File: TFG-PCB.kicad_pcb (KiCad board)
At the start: 2 copper layers, 287.3 x 99.2 mm, 141 parts, among them J1 TYPE-C-31-M-12, SW1 SW_Push, U1 ATmega32U4-AU, Y1 16MHz

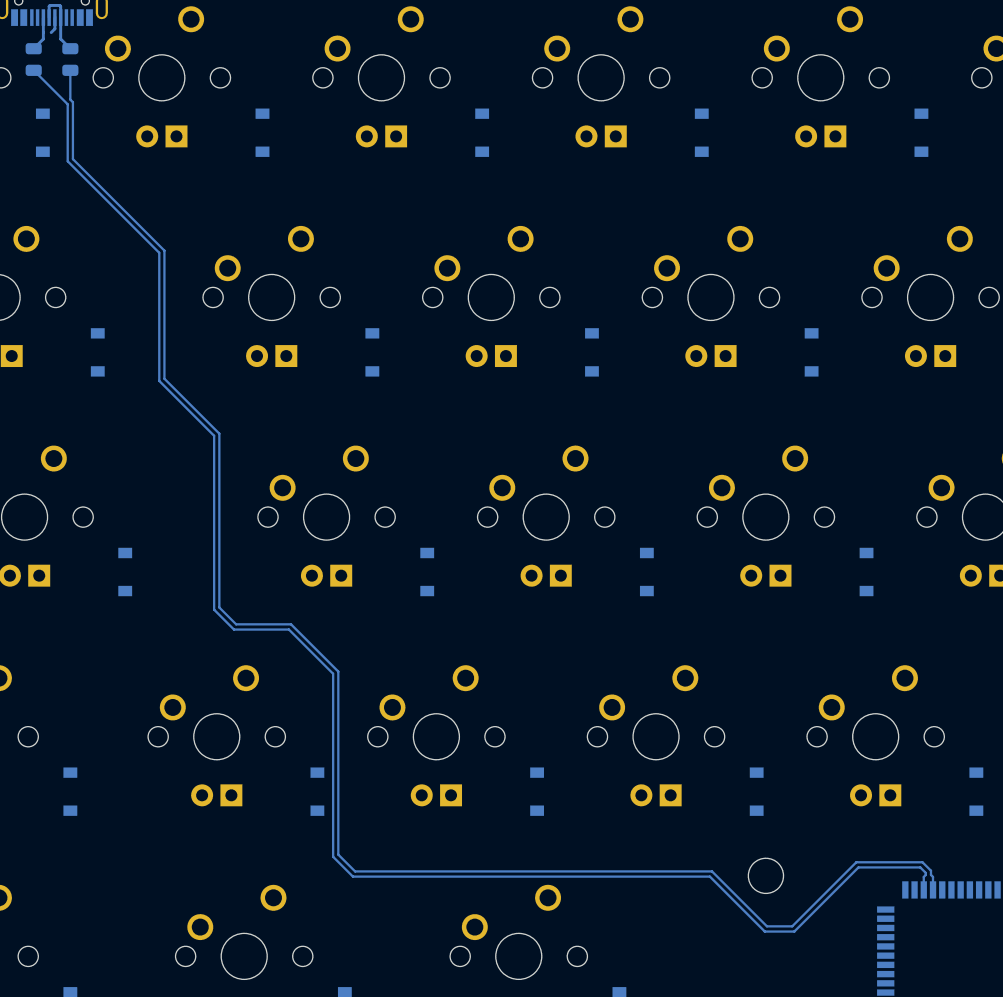
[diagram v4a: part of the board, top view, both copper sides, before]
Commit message: Wired USB
Finished differential wiring + skew
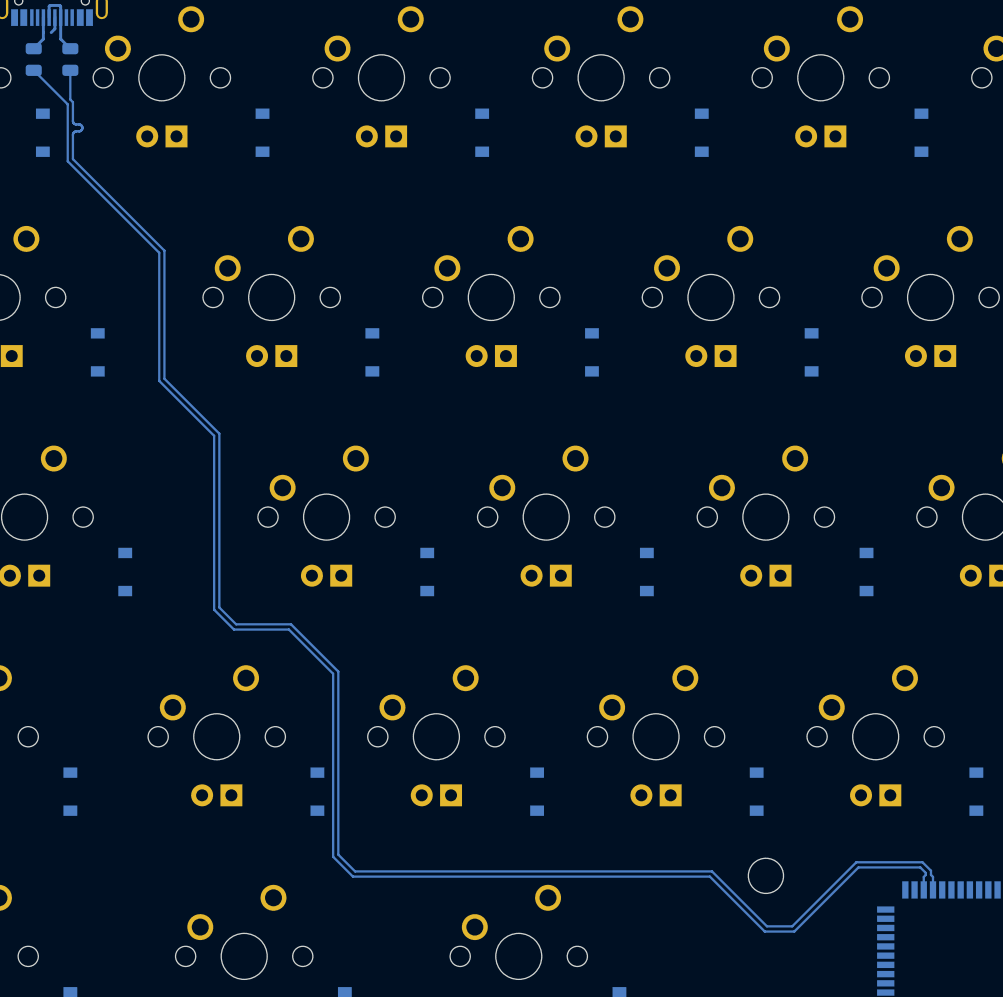
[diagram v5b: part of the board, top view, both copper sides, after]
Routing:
- net /D_P: track 138.8 -> 139.9 mm
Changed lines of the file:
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@@
     (thickness 1.6)
     (drawings 466)
-    (tracks 64)
+    (tracks 95)
     (zones 0)
     (modules 141)
@@
   (segment (start 222.25 237.98125) (end 225.28125 237.98125) (width 0.254) (layer B.Cu) (net 44))
   (segment (start 225.28125 237.98125) (end 226.275 238.975) (width 0.254) (layer B.Cu) (net 44))
-  (segment (start 150.11195 211.70625) (end 148.65625 210.25055) (width 0.2) (layer B.Cu) (net 122))
-  (segment (start 154.87445 211.70625) (end 150.11195 211.70625) (width 0.2) (layer B.Cu) (net 122))
-  (segment (start 158.975 215.8068) (end 154.87445 211.70625) (width 0.2) (layer B.Cu) (net 122))
-  (segment (start 158.975 231.6818) (end 158.975 215.8068) (width 0.2) (layer B.Cu) (net 122))
-  (segment (start 160.4307 233.1375) (end 158.975 231.6818) (width 0.2) (layer B.Cu) (net 122))
-  (segment (start 198.3443 237.9) (end 196.14945 237.9) (width 0.2) (layer B.Cu) (net 122))
-  (segment (start 203.90055 232.34375) (end 198.3443 237.9) (width 0.2) (layer B.Cu) (net 122))
-  (segment (start 209.6432 232.34375) (end 203.90055 232.34375) (width 0.2) (layer B.Cu) (net 122))
-  (segment (start 191.38695 233.1375) (end 160.4307 233.1375) (width 0.2) (layer B.Cu) (net 122))
-  (segment (start 143.89375 179.2943) (end 135.95625 171.3568) (width 0.2) (layer B.Cu) (net 122))
-  (segment (start 210.5535 234.74275) (end 210.5535 233.617749) (width 0.2) (layer B.Cu) (net 122))
-  (segment (start 210.5535 233.617749) (end 210.3785 233.442749) (width 0.2) (layer B.Cu) (net 122))
-  (segment (start 210.3785 233.442749) (end 210.3785 233.07905) (width 0.2) (layer B.Cu) (net 122))
-  (segment (start 210.3785 233.07905) (end 209.6432 232.34375) (width 0.2) (layer B.Cu) (net 122))
-  (segment (start 148.65625 210.25055) (end 148.65625 195.1693) (width 0.2) (layer B.Cu) (net 122))
-  (segment (start 196.14945 237.9) (end 191.38695 233.1375) (width 0.2) (layer B.Cu) (net 122))
-  (segment (start 148.65625 195.1693) (end 143.89375 190.4068) (width 0.2) (layer B.Cu) (net 122))
-  (segment (start 143.89375 190.4068) (end 143.89375 179.2943) (width 0.2) (layer B.Cu) (net 122))
-  (segment (start 135.95625 171.3568) (end 135.95625 166.419853) (width 0.2) (layer B.Cu) (net 122))
-  (segment (start 135.95625 166.419853) (end 135.73125 166.194853) (width 0.2) (layer B.Cu) (net 122))
-  (segment (start 135.73125 166.194853) (end 135.73125 163.65625) (width 0.2) (layer B.Cu) (net 122))
+  (segment (start 158.975 231.6818) (end 160.4307 233.1375) (width 0.2) (layer B.Cu) (net 122))
+  (segment (start 209.6432 232.34375) (end 210.3785 233.07905) (width 0.2) (layer B.Cu) (net 122))
+  (segment (start 158.975 215.8068) (end 158.975 231.6818) (width 0.2) (layer B.Cu) (net 122))
+  (segment (start 196.14945 237.9) (end 198.3443 237.9) (width 0.2) (layer B.Cu) (net 122))
+  (segment (start 154.87445 211.70625) (end 158.975 215.8068) (width 0.2) (layer B.Cu) (net 122))
+  (segment (start 150.11195 211.70625) (end 154.87445 211.70625) (width 0.2) (layer B.Cu) (net 122))
+  (segment (start 210.5535 233.617749) (end 210.5535 234.74275) (width 0.2) (layer B.Cu) (net 122))
+  (segment (start 148.65625 210.25055) (end 150.11195 211.70625) (width 0.2) (layer B.Cu) (net 122))
+  (segment (start 143.89375 190.4068) (end 148.65625 195.1693) (width 0.2) (layer B.Cu) (net 122))
+  (segment (start 136.714674 168.462953) (end 136.750415 168.519834) (width 0.2) (layer B.Cu) (net 122))
+  (segment (start 136.667171 168.41545) (end 136.714674 168.462953) (width 0.2) (layer B.Cu) (net 122))
+  (segment (start 136.480124 168.35) (end 136.546881 168.357521) (width 0.2) (layer B.Cu) (net 122))
+  (segment (start 136.069204 168.284549) (end 136.126085 168.32029) (width 0.2) (layer B.Cu) (net 122))
+  (segment (start 136.25625 168.35) (end 136.480124 168.35) (width 0.2) (layer B.Cu) (net 122))
+  (segment (start 136.126085 168.32029) (end 136.189494 168.342478) (width 0.2) (layer B.Cu) (net 122))
+  (segment (start 203.90055 232.34375) (end 209.6432 232.34375) (width 0.2) (layer B.Cu) (net 122))
+  (segment (start 136.546881 168.357521) (end 136.61029 168.379709) (width 0.2) (layer B.Cu) (net 122))
+  (segment (start 198.3443 237.9) (end 203.90055 232.34375) (width 0.2) (layer B.Cu) (net 122))
+  (segment (start 136.189494 168.342478) (end 136.25625 168.35) (width 0.2) (layer B.Cu) (net 122))
+  (segment (start 148.65625 195.1693) (end 148.65625 210.25055) (width 0.2) (layer B.Cu) (net 122))
+  (segment (start 135.95625 166.419853) (end 135.95625 168.05) (width 0.2) (layer B.Cu) (net 122))
+  (segment (start 136.772603 168.583243) (end 136.780124 168.65) (width 0.2) (layer B.Cu) (net 122))
+  (segment (start 136.61029 168.379709) (end 136.667171 168.41545) (width 0.2) (layer B.Cu) (net 122))
+  (segment (start 136.069204 169.01545) (end 136.021701 169.062953) (width 0.2) (layer B.Cu) (net 122))
+  (segment (start 136.546881 168.942478) (end 136.480124 168.95) (width 0.2) (layer B.Cu) (net 122))
+  (segment (start 135.98596 169.119834) (end 135.963772 169.183243) (width 0.2) (layer B.Cu) (net 122))
+  (segment (start 135.98596 168.180165) (end 136.021701 168.237046) (width 0.2) (layer B.Cu) (net 122))
+  (segment (start 210.3785 233.442749) (end 210.5535 233.617749) (width 0.2) (layer B.Cu) (net 122))
+  (segment (start 136.126085 168.979709) (end 136.069204 169.01545) (width 0.2) (layer B.Cu) (net 122))
+  (segment (start 136.750415 168.519834) (end 136.772603 168.583243) (width 0.2) (layer B.Cu) (net 122))
+  (segment (start 135.73125 163.65625) (end 135.73125 166.194853) (width 0.2) (layer B.Cu) (net 122))
+  (segment (start 136.780124 168.65) (end 136.772603 168.716756) (width 0.2) (layer B.Cu) (net 122))
+  (segment (start 191.38695 233.1375) (end 196.14945 237.9) (width 0.2) (layer B.Cu) (net 122))
+  (segment (start 136.772603 168.716756) (end 136.750415 168.780165) (width 0.2) (layer B.Cu) (net 122))
+  (segment (start 136.750415 168.780165) (end 136.714674 168.837046) (width 0.2) (layer B.Cu) (net 122))
+  (segment (start 136.714674 168.837046) (end 136.667171 168.884549) (width 0.2) (layer B.Cu) (net 122))
+  (segment (start 136.667171 168.884549) (end 136.61029 168.92029) (width 0.2) (layer B.Cu) (net 122))
+  (segment (start 135.963772 168.116756) (end 135.98596 168.180165) (width 0.2) (layer B.Cu) (net 122))
+  (segment (start 136.61029 168.92029) (end 136.546881 168.942478) (width 0.2) (layer B.Cu) (net 122))
+  (segment (start 160.4307 233.1375) (end 191.38695 233.1375) (width 0.2) (layer B.Cu) (net 122))
+  (segment (start 136.480124 168.95) (end 136.25625 168.95) (width 0.2) (layer B.Cu) (net 122))
+  (segment (start 135.95625 168.05) (end 135.963772 168.116756) (width 0.2) (layer B.Cu) (net 122))
+  (segment (start 136.25625 168.95) (end 136.189494 168.957521) (width 0.2) (layer B.Cu) (net 122))
+  (segment (start 210.3785 233.07905) (end 210.3785 233.442749) (width 0.2) (layer B.Cu) (net 122))
+  (segment (start 136.189494 168.957521) (end 136.126085 168.979709) (width 0.2) (layer B.Cu) (net 122))
+  (segment (start 135.73125 166.194853) (end 135.95625 166.419853) (width 0.2) (layer B.Cu) (net 122))
+  (segment (start 136.021701 169.062953) (end 135.98596 169.119834) (width 0.2) (layer B.Cu) (net 122))
+  (segment (start 136.021701 168.237046) (end 136.069204 168.284549) (width 0.2) (layer B.Cu) (net 122))
+  (segment (start 135.963772 169.183243) (end 135.95625 169.25) (width 0.2) (layer B.Cu) (net 122))
+  (segment (start 135.95625 169.25) (end 135.95625 171.3568) (width 0.2) (layer B.Cu) (net 122))
+  (segment (start 135.95625 171.3568) (end 143.89375 179.2943) (width 0.2) (layer B.Cu) (net 122))
+  (segment (start 143.89375 179.2943) (end 143.89375 190.4068) (width 0.2) (layer B.Cu) (net 122))
   (segment (start 135.50625 166.60625) (end 132.55625 163.65625) (width 0.2) (layer B.Cu) (net 123))
   (segment (start 143.44375 190.5932) (end 143.44375 179.4807) (width 0.2) (layer B.Cu) (net 123))

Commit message: Rewiring + moving diodes
Moved diodes (for the last time i think) and started wiring MC
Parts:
- moved C4 79.1 mm to (205.9, 232.3)
- moved C5 68.9 mm to (213.1, 230.8), turned to 90 degrees
- moved C3 51.4 mm to (217.9, 231.1)
- moved C7 41.8 mm to (216.4, 249.0), turned to 0 degrees
- moved C6 41.7 mm to (221.4, 233.9), turned to 90 degrees
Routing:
- net +5V: track 0.00 -> 30.6 mm, vias 0 -> 4
- net /D_N: track 139.9 -> 131.2 mm
- net /D_P: track 139.9 -> 131.2 mm

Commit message: Almost all wiring done
Practically finished wiring
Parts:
- added C8: 1uF, Capacitor_SMD:C_0805_2012Metric, B.Cu at (204.1, 237.2)
- added C9: 1uF, Capacitor_SMD:C_0805_2012Metric, B.Cu at (214.0, 232.3)
- F1, R4: moved to B.Cu
- moved R5 58.8 mm to (203.5, 248.8)
- moved SW1 33.2 mm to (267.7, 235.3), turned to 90 degrees
- moved F1 30.2 mm to (138.7, 168.1), turned to 90 degrees
- moved R1 27.8 mm to (273.8, 232.4)
- moved R4 18.1 mm to (140.5, 157.1), turned to 90 degrees
- moved C5 16.8 mm to (203.3, 244.5), turned to 180 degrees
- moved C3 6.48 mm to (211.6, 229.9), turned to 180 degrees
- moved D54 0.79 mm to (382.6, 226.2)
- moved C7 0.38 mm to (216.4, 248.7)
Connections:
- U1 pad 42: Net-(U1-Pad42) -> +5V
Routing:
- net ROW4: track 0.00 -> 266.4 mm
- net ROW1: track 0.00 -> 263.5 mm, vias 0 -> 2
- net ROW0: track 0.00 -> 257.6 mm, vias 0 -> 2
- net ROW3: track 0.00 -> 247.3 mm, vias 0 -> 2
- net ROW2: track 0.00 -> 235.7 mm, vias 0 -> 2
- net GND: track 0.00 -> 184.6 mm
- net +5V: track 30.6 -> 214.1 mm, vias 4 -> 7
- net COL2: track 0.00 -> 90.1 mm, vias 0 -> 2
- net COL12: track 0.00 -> 90.0 mm
- net COL10: track 0.00 -> 89.0 mm
- net COL11: track 0.00 -> 88.0 mm
- net COL6: track 0.00 -> 88.0 mm
- net COL1: track 0.00 -> 87.6 mm, vias 0 -> 6
- net COL0: track 0.00 -> 83.0 mm
- net COL13: track 0.00 -> 82.3 mm
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
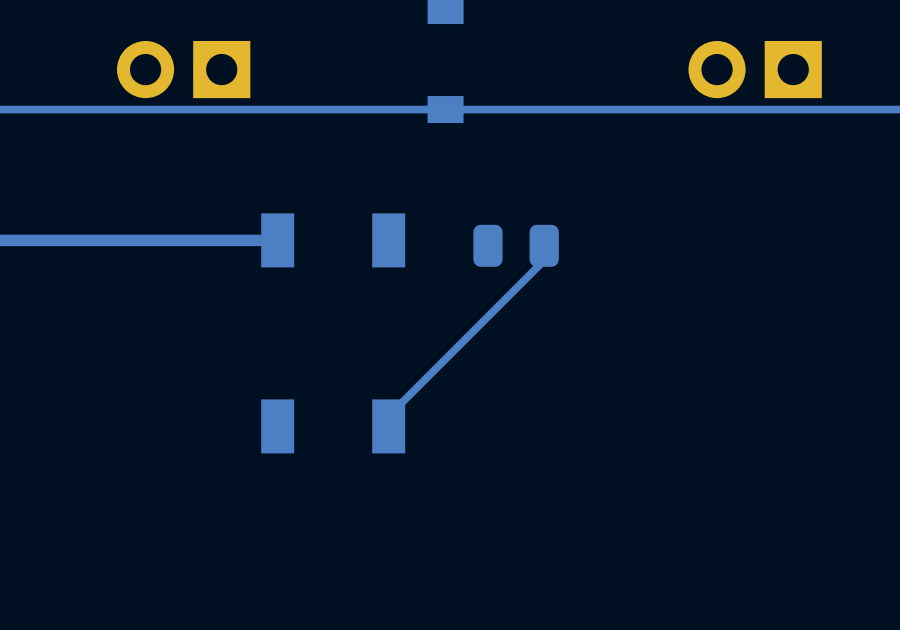
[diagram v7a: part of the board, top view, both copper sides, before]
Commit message: Remade Reset button circuit
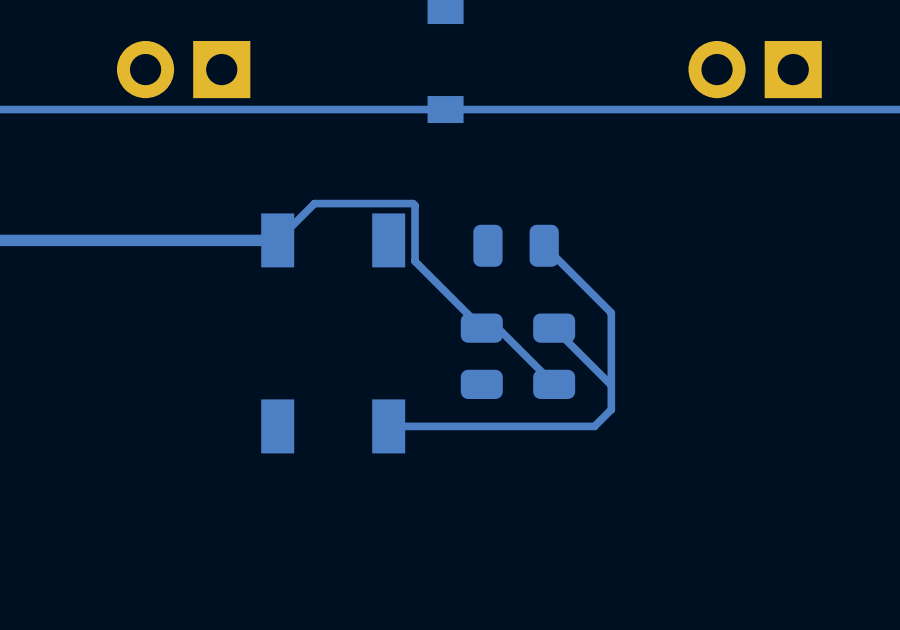
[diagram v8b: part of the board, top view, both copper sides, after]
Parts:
- added C10: 22pF, Capacitor_SMD:C_0805_2012Metric, B.Cu at (275.1, 236.1)
- added R6: 330, Resistor_SMD:R_0805_2012Metric, B.Cu at (272.7, 236.1)
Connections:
- net Net-(R1-Pad2) renamed RST
- R1 pad 1: +5V -> Net-(R1-Pad1)
- SW1 pad 1: GND -> Net-(R6-Pad1)
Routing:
- net Net-(C10-Pad2): track 0.00 -> 12.8 mm
- net RST: track 8.17 -> 17.6 mm
